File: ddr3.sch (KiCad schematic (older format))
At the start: 60 parts, among them U7 AS4C256M16D3, U8 TPS51200DRC

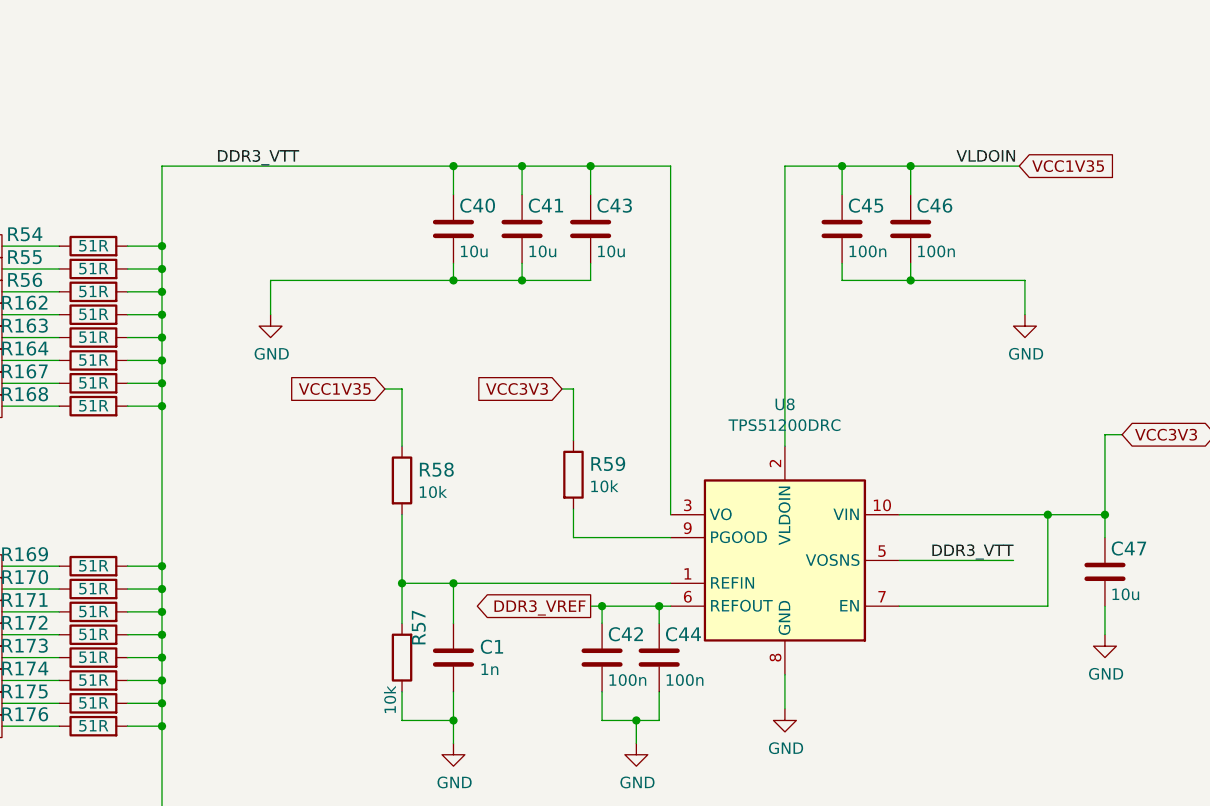
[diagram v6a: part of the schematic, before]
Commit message: Update layout around filtering caps
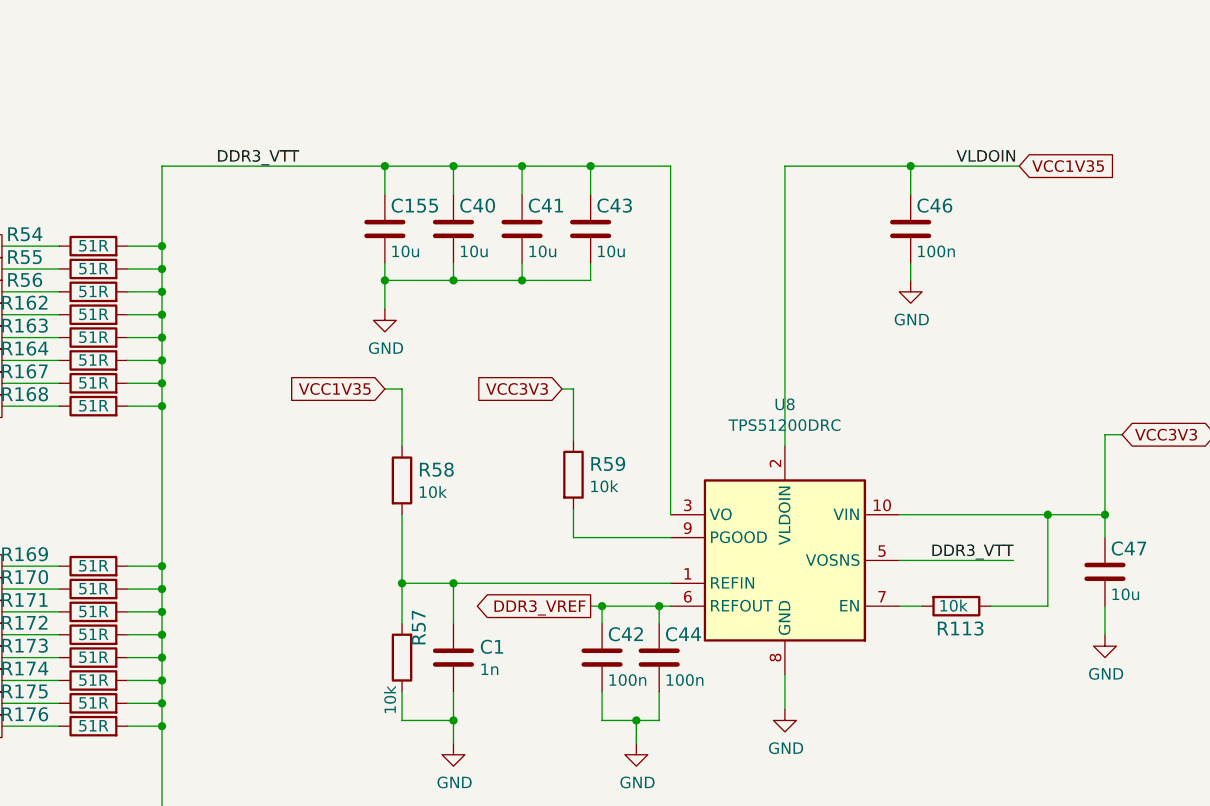
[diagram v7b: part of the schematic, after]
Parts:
- removed C45: C_100n_0402, artix-dc-scm-footprints:0402-cap, symbol artix-dc-scm:C_100n_0402-artix-dc-scm
- added C155: C_10u_0402, artix-dc-scm-footprints:0402-cap, symbol artix-dc-scm:C_10u_0402
- added R113: R_10k_0402, artix-dc-scm-footprints:0402-res, symbol artix-dc-scm:R_10k_0402
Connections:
- net DDR3_VTT: now also C155.1
- net GND: now also C155.2
- net VCC3V3: now also R113.1; no longer U8.7 (EN)
- new net: R113.2, U8.7 (EN)
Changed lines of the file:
@@
 L artix-dc-scm:GND-artix-dc-scm #PWR036
 U 1 1 617E94FA
-P 5600 7675
-F 0 "#PWR036" H 5600 7425 50  0001 C CNN
-F 1 "GND" H 5605 7502 50  0000 C CNN
-F 2 "" H 5600 7675 50  0001 C CNN
-F 3 "" H 5600 7675 50  0001 C CNN
-	1    5600 7675
+P 6100 7650
+F 0 "#PWR036" H 6100 7400 50  0001 C CNN
+F 1 "GND" H 6105 7477 50  0000 C CNN
+F 2 "" H 6100 7650 50  0001 C CNN
+F 3 "" H 6100 7650 50  0001 C CNN
+	1    6100 7650
 	1    0    0    -1
 $EndComp
@@
 Wire Wire Line
 	7000 7450 7000 7525
-Wire Wire Line
-	8100 7025 8400 7025
 Connection ~ 8400 7025
-Wire Wire Line
-	8400 7525 8100 7525
 $Comp
 L artix-dc-scm:GND-artix-dc-scm #PWR040
 U 1 1 61880049
-P 8900 7675
-F 0 "#PWR040" H 8900 7425 50  0001 C CNN
-F 1 "GND" H 8905 7502 50  0000 C CNN
-F 2 "" H 8900 7675 50  0001 C CNN
-F 3 "" H 8900 7675 50  0001 C CNN
-	1    8900 7675
-	1    0    0    -1
-$EndComp
-Wire Wire Line
-	8100 7025 8100 7150
+P 8400 7525
+F 0 "#PWR040" H 8400 7275 50  0001 C CNN
+F 1 "GND" H 8405 7352 50  0000 C CNN
+F 2 "" H 8400 7525 50  0001 C CNN
+F 3 "" H 8400 7525 50  0001 C CNN
+	1    8400 7525
+	1    0    0    -1
+$EndComp
 Wire Wire Line
 	8400 7025 8400 7150
-$Comp
-L artix-dc-scm:C_100n_0402-artix-dc-scm C?
-U 1 1 60AEFC4F
-P 8100 7300
-AR Path="/60AEFC4F" Ref="C?"  Part="1"
-AR Path="/5FD8EBC2/60AEFC4F" Ref="C45"  Part="1"
-F 0 "C45" H 8125 7400 60  0000 L CNN
-F 1 "C_100n_0402" H 8100 7150 60  0001 C CNN
-F 2 "artix-dc-scm-footprints:0402-cap" H 8300 7500 60  0001 L CNN
-F 3 "" H 8100 7300 50  0001 C CNN
-F 4 "Walsin" H 8300 7700 60  0001 L CNN "Manufacturer"
-F 5 "0402X104K6R3CT" H 8300 7600 60  0001 L CNN "MPN"
-F 6 "100n" H 8125 7200 50  0000 L CNN "Val"
-	1    8100 7300
-	1    0    0    -1
-$EndComp
-Wire Wire Line
-	8100 7450 8100 7525
 Wire Wire Line
 	8400 7450 8400 7525
 Wire Wire Line
-	8400 7525 8900 7525
-Wire Wire Line
-	8900 7525 8900 7675
-Connection ~ 8400 7525
-Wire Wire Line
 	8400 7025 8875 7025
 Wire Wire Line
@@
 	6925 8000 6875 8000
 Wire Wire Line
-	6400 7525 5600 7525
-Wire Wire Line
-	5600 7525 5600 7675
+	6400 7525 6100 7525
+Wire Wire Line
+	6100 7525 6100 7650
 Connection ~ 6400 7525
 Text Label 8600 7025 0    50   ~ 0
@@
 	0    1    1    0
 $EndComp
-Wire Wire Line
-	7850 7025 8100 7025
-Connection ~ 8100 7025
 Connection ~ 7000 7025
 Wire Wire Line
@@
 $EndComp
 Wire Wire Line
-	5125 7025 6400 7025
+	5125 7025 6100 7025
 Text Label 5725 7025 2    50   ~ 0
 DDR3_VTT
@@
 VCC3V3
 Wire Wire Line
-	8350 8950 9000 8950
-Wire Wire Line
 	9000 8950 9000 8550
 Connection ~ 9000 8550
@@
 	1    0    0    -1
 $EndComp
+$Comp
+L artix-dc-scm:R_10k_0402 R113
+U 1 1 5FFC6E4F
+P 8600 8950
+F 0 "R113" H 8475 9050 60  0000 L CNN
+F 1 "R_10k_0402" H 8600 8800 60  0001 C CNN
+F 2 "artix-dc-scm-footprints:0402-res" H 8800 9150 60  0001 L CNN
+F 3 "" H 8600 8950 50  0001 C CNN
+F 4 "VISHAY" H 8800 9350 60  0001 L CNN "Manufacturer"
+F 5 "CRCW040210K0FKEDHP" H 8800 9250 60  0001 L CNN "MPN"
+F 6 "10k" H 8550 8950 50  0000 L CNN "Val"
+	1    8600 8950
+	-1   0    0    1
+$EndComp
+Wire Wire Line
+	8350 8950 8450 8950
+Wire Wire Line
+	8750 8950 9000 8950
+$Comp
+L artix-dc-scm:C_10u_0402 C155
+U 1 1 60068359
+P 6100 7300
+F 0 "C155" H 6125 7400 60  0000 L CNN
+F 1 "C_10u_0402" H 6100 7150 60  0001 C CNN
+F 2 "artix-dc-scm-footprints:0402-cap" H 6300 7500 60  0001 L CNN
+F 3 "" H 6100 7300 50  0001 C CNN
+F 4 "MURATA" H 6300 7700 60  0001 L CNN "Manufacturer"
+F 5 "GRM155R60J106ME44D" H 6300 7600 60  0001 L CNN "MPN"
+F 6 "10u" H 6125 7200 50  0000 L CNN "Val"
+	1    6100 7300
+	1    0    0    -1
+$EndComp
+Wire Wire Line
+	6100 7150 6100 7025
+Connection ~ 6100 7025
+Wire Wire Line
+	6100 7025 6400 7025
+Wire Wire Line
+	6100 7450 6100 7525
+Connection ~ 6100 7525
+Wire Wire Line
+	7850 7025 8400 7025
 $EndSCHEMATC

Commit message: Generated local libs
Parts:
- R162, R163, R164, R167, R168, R169, R170, R171, R172, R173, R174, R175, R176, R177, R178, R179, R180, R181, R182, R183, R184, R54, R55, R56: footprint antmicro-footprints:0402-res -> artix-dc-scm-footprints:0402-res; symbol antmicroResistors0402:R_51R_0402 -> artix-dc-scm:R_51R_0402
